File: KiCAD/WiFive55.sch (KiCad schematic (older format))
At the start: 53 parts, among them J2 Switched Output, J3 Breadboard, J4 Grounds, J5 555-esque, K1 FINDER-36.11, Q1 BS170, Q2 IRF540N, Q5 BC557, SW3 PRG, SW6 RST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

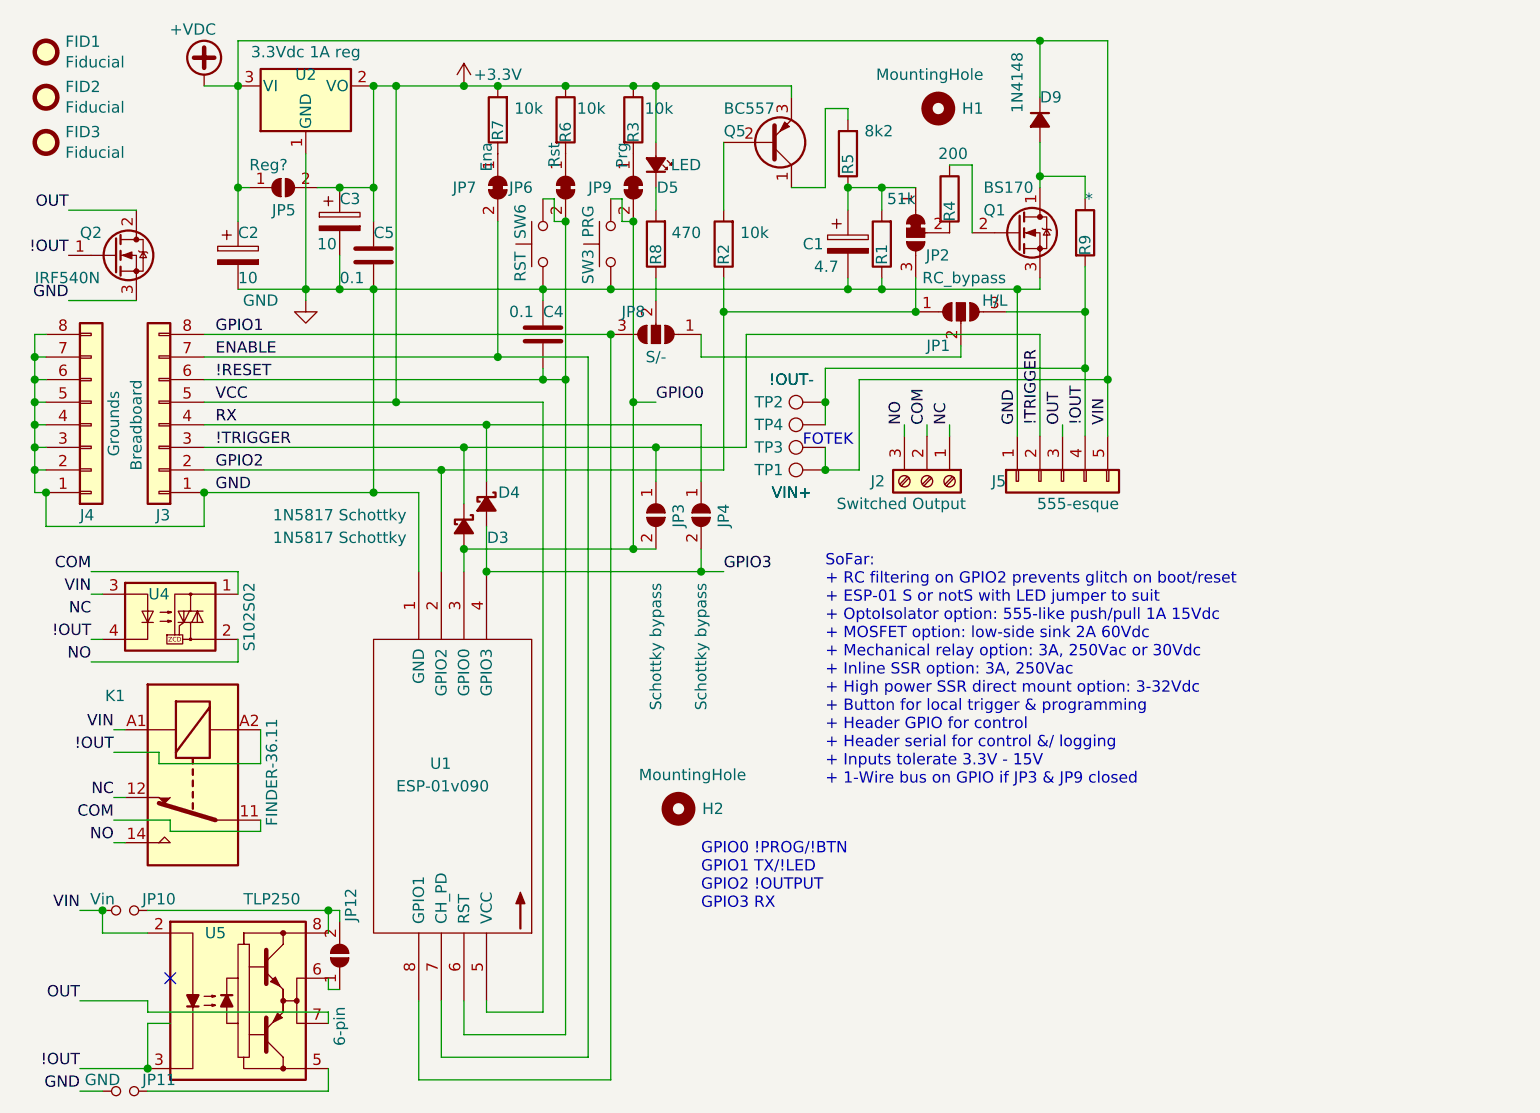
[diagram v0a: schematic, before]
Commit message: update PCB for multiple SSR/RLA options
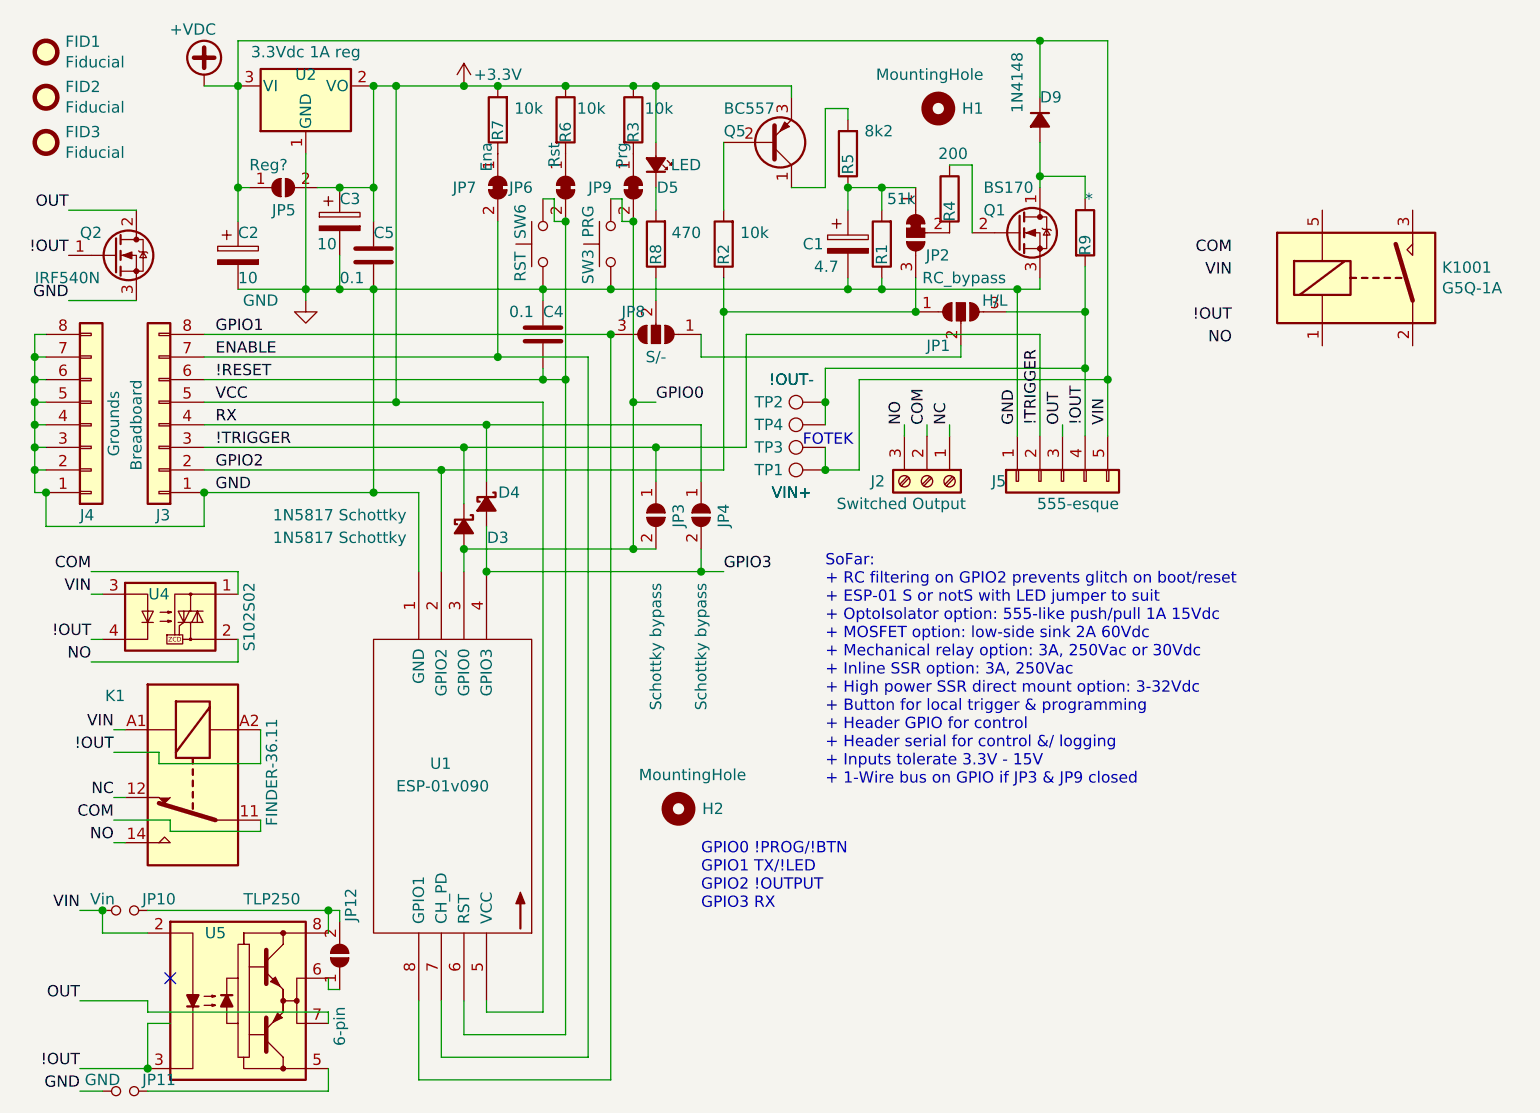
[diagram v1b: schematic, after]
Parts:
- added K1001: G5Q-1A, Relay_THT:Relay_SPST_TE_PCN-1xxD3MHZ, symbol Relay:G5Q-1A
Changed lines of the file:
@@
 Sheet 1 1
 Title "WiFive55"
-Date "2021-04-02"
-Rev "0.10"
+Date "2021-04-13"
+Rev "0.11"
 Comp "(c)2021 Phill Rogers @ TechColab.co.je"
 Comment1 ""
@@
 Text Label 900  3050 2    50   ~ 0
 VIN
-Text Label 900  3150 2    50   ~ 0
-NC
 Text Label 900  2950 2    50   ~ 0
 COM
@@
 Wire Wire Line
 	1400 2400 2550 2400
+$Comp
+L Relay:G5Q-1A K1001
+U 1 1 60754CB2
+P 6550 1650
+F 0 "K1001" H 6880 1696 50  0000 L CNN
+F 1 "G5Q-1A" H 6880 1605 50  0000 L CNN
+F 2 "Relay_THT:Relay_SPST_TE_PCN-1xxD3MHZ" H 6900 1600 50  0001 L CNN
+F 3 "https://www.omron.com/ecb/products/pdf/en-g5q.pdf" H 6550 1650 50  0001 C CNN
+	1    6550 1650
+	1    0    0    -1
+$EndComp
+Text Label 5950 1850 2    50   ~ 0
+!OUT
+Text Label 5950 1650 2    50   ~ 0
+VIN
+Text Label 5950 1550 2    50   ~ 0
+COM
+Text Label 5950 1950 2    50   ~ 0
+NO
 $EndSCHEMATC
